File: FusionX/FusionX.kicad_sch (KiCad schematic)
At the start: 1 part, among them U1 SC600YNAPA-E53-UGADA

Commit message: Updated sheet
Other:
- company: (none) -> NoahGWood
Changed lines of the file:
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@@
     (date "2023-08-15")
     (rev "1")
+    (company "NoahGWood")
     (comment 1 "License: The Unlicense")
-    (comment 3 "Twitch.tv")
+    (comment 2 "twitch.tv/u/noahgwood")
+    (comment 3 "Developed Live On:")
     (comment 4 "SC600Y Based Smartphone")
   )

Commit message: Finished RaspiLCD Added Antennas Started secondary LCD
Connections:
- net ANT_WIFI: now reaches U1.129 (ANT_WIFI/BT)
- net ANT_GNSS: now reaches U1.134 (ANT_GNSS)
- net ANT_DRX: now reaches U1.149 (ANT_DRX)
- net LDO6_1P8: now reaches U1.10 (LDO6_1P8)
- net LDO10_2P8: now reaches U1.11 (LDO10_2P8)
- net LDO17_2P85: now reaches U1.12 (LDO17_2P85)
- net LDO2_1P1: now reaches U1.13 (LDO2_1P1)
- net LDO22_2P8: now reaches U1.14 (LDO22_2P8)
- net LDO23_1P2: now reaches U1.15 (LDO23_1P2)
- net VRTC: now reaches U1.16 (VRTC)
- net ANT_MAIN: now reaches U1.19 (ANT_MAIN)
- net +BATT: now reaches U1.27 (BAT_PLUS)
- net -BATT: now reaches U1.28 (BAT_MINUS)
- net BAT_THERM: now reaches U1.29 (BAT_THERM)
- net VBAT: now reaches U1.36 (VBAT)
- net VBAT: now also U1.37 (VBAT), U1.38 (VBAT)
- net LDO5_1P8: now reaches U1.9 (LDO5_1P8)
- net ANT_FM: now reaches U1.244 (ANT_FM)
- no-connect marks 2 -> 4
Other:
- sheet LCD renamed RaspiLCD
- added sheet OtherLCD (OtherLCD.kicad_sch)
- added sheet RF (RF.kicad_sch)
- sheet RaspiLCD: file LCD.kicad_sch -> RaspiLCD.kicad_sch
- moved on the sheet: U1A, U1B, U1C

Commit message: Implemented: 	USB-C Super Speed 	Capacitve Touch Screen 	Secondary LCD
Started On:
	PCB Layout
	Case Design
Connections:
- net USB_SS_RX_P: now reaches U1.171 (USB_SS_RX_P)
- net USB_SS_RX_M: now reaches U1.172 (USB_SS_RX_M)
- net USB_SS_TX_P: now reaches U1.174 (USB_SS_TX__P)
- net USB_SS_TX_M: now reaches U1.175 (USB_SS_TX__M)
- net USB_OPT: now reaches U1.217 (USB_OPT)
- net USB_CC2: now reaches U1.223 (USBC_CC2)
- net USB_CC1: now reaches U1.224 (USBC_CC1)
- net USB_SS_SEL: now reaches U1.226 (USB_SS_SEL)
- net USB_ID: now reaches U1.30 (USB_ID)
- net USB_DP: now reaches U1.32 (USB_DP)
- net USB_DM: now reaches U1.33 (USB_DM)
- net USB_OTG_ON: now reaches U1.247 (GPIO_1)
- net USB_SS_ON: now reaches U1.248 (GPIO_0)
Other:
- added sheet USB (USB.kicad_sch)
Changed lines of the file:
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@@
   (title_block
     (title "FusionX")
-    (date "2023-08-15")
+    (date "2023-08-17")
     (rev "1")
     (company "NoahGWood")
@@
     (stroke (width 0) (type default))
   )
+  (wire (pts (xy 71.755 158.115) (xy 78.105 158.115))
+    (stroke (width 0) (type default))
+  )
   (wire (pts (xy 480.695 204.47) (xy 480.695 207.01))
     (stroke (width 0) (type default))
@@
     (stroke (width 0) (type default))
   )
+  (wire (pts (xy 365.125 156.845) (xy 358.775 156.845))
+    (stroke (width 0) (type default))
+  )
   (wire (pts (xy 531.495 209.55) (xy 531.495 212.09))
     (stroke (width 0) (type default))
@@
     (stroke (width 0) (type default))
   )
+  (wire (pts (xy 365.125 133.985) (xy 358.775 133.985))
+    (stroke (width 0) (type default))
+  )
   (wire (pts (xy 531.495 204.47) (xy 531.495 207.01))
     (stroke (width 0) (type default))
@@
     (stroke (width 0) (type default))
   )
+  (wire (pts (xy 71.755 160.655) (xy 78.105 160.655))
+    (stroke (width 0) (type default))
+  )
   (wire (pts (xy 285.115 303.53) (xy 278.765 303.53))
     (stroke (width 0) (type default))
@@
     (stroke (width 0) (type default))
   )
+  (wire (pts (xy 365.125 141.605) (xy 358.775 141.605))
+    (stroke (width 0) (type default))
+  )
   (wire (pts (xy 480.695 194.31) (xy 480.695 196.85))
     (stroke (width 0) (type default))
@@
     (stroke (width 0) (type default))
   )
+  (wire (pts (xy 71.755 153.035) (xy 78.105 153.035))
+    (stroke (width 0) (type default))
+  )
+  (wire (pts (xy 281.305 118.745) (xy 287.655 118.745))
+    (stroke (width 0) (type default))
+  )
+  (wire (pts (xy 365.125 139.065) (xy 358.775 139.065))
+    (stroke (width 0) (type default))
+  )
   (wire (pts (xy 480.695 232.41) (xy 480.695 234.95))
     (stroke (width 0) (type default))
@@
     (stroke (width 0) (type default))
   )
+  (wire (pts (xy 281.305 113.665) (xy 287.655 113.665))
+    (stroke (width 0) (type default))
+  )
   (wire (pts (xy 196.215 331.47) (xy 202.565 331.47))
     (stroke (width 0) (type default))
@@
     (stroke (width 0) (type default))
   )
+  (wire (pts (xy 281.305 111.125) (xy 287.655 111.125))
+    (stroke (width 0) (type default))
+  )
   (wire (pts (xy 531.495 171.45) (xy 531.495 173.99))
     (stroke (width 0) (type default))
   )
+  (wire (pts (xy 281.305 121.285) (xy 287.655 121.285))
+    (stroke (width 0) (type default))
+  )
   (wire (pts (xy 531.495 224.79) (xy 531.495 227.33))
     (stroke (width 0) (type default))
@@
     (stroke (width 0) (type default))
   )
-  (text_box "TODO:\n	[ ] Microphone\n	[ ] Speaker(s)\n	[ ] Headphone Jack\n	[ ] Antennas\n	[ ] USB-C 3.0\n	[ ] uSIM\n	[ ] SD Card\n	[X] Main LCD\n	[ ] Front Camera\n	[ ] Rear Camera\n	[ ] *Depth Camera\n	[ ] *Secondary Screen\n	[ ] Capacitive Touch\n	[ ] Ambient Light Sensor\n	[ ] Accelerometer\n	[ ] Compass"
+  (text_box "TODO:\n	[ ] Microphone\n	[ ] Speaker(s)\n	[ ] Headphone Jack\n	[X] Antennas\n	[X] USB-C 3.0\n	[ ] uSIM\n	[ ] SD Card\n	[X] Main LCD\n	[ ] Front Camera\n	[ ] Rear Camera\n	[ ] *Depth Camera\n	[ ] *Secondary Screen\n	[X] Capacitive Touch\n	[ ] Ambient Light Sensor\n	[ ] Accelerometer\n	[ ] Compass"
     (at 167.64 47.625 0) (size 66.675 72.39)
     (stroke (width 0) (type default))
     (fill (type none))
     (effects (font (size 2.5 2.5)) (justify left top))
+  )
+  (global_label "USB_SS_TX_M" (shape input) (at 281.305 121.285 180) (fields_autoplaced)
+    (effects (font (size 1.27 1.27)) (justify right))
+    (property "Intersheetrefs" "${INTERSHEET_REFS}" (at 265.5595 121.285 0)
+      (effects (font (size 1.27 1.27)) (justify right) hide)
+    )
+  )
+  (global_label "USB_SS_RX_P" (shape input) (at 281.305 111.125 180) (fields_autoplaced)
+    (effects (font (size 1.27 1.27)) (justify right))
+    (property "Intersheetrefs" "${INTERSHEET_REFS}" (at 265.4385 111.125 0)
+      (effects (font (size 1.27 1.27)) (justify right) hide)
+    )
   )
   (global_label "ANT_GNSS" (shape input) (at 285.115 318.77 0) (fields_autoplaced)
@@
     )
   )
+  (global_label "USB_SS_TX_P" (shape input) (at 281.305 118.745 180) (fields_autoplaced)
+    (effects (font (size 1.27 1.27)) (justify right))
+    (property "Intersheetrefs" "${INTERSHEET_REFS}" (at 265.7409 118.745 0)
+      (effects (font (size 1.27 1.27)) (justify right) hide)
+    )
+  )
   (global_label "VRTC" (shape input) (at 78.105 117.475 180) (fields_autoplaced)
     (effects (font (size 1.27 1.27)) (justify right))
@@
     )
   )
+  (global_label "USB_SS_ON" (shape input) (at 480.695 146.05 180) (fields_autoplaced)
+    (effects (font (size 1.27 1.27)) (justify right))
+    (property "Intersheetrefs" "${INTERSHEET_REFS}" (at 466.8846 146.05 0)
+      (effects (font (size 1.27 1.27)) (justify right) hide)
+    )
+  )
   (global_label "DSI0_LN3_N" (shape output) (at 285.115 344.17 0) (fields_autoplaced)
     (effects (font (size 1.27 1.27)) (justify left))
@@
     )
   )
+  (global_label "USB_SS_RX_M" (shape input) (at 281.305 113.665 180) (fields_autoplaced)
+    (effects (font (size 1.27 1.27)) (justify right))
+    (property "Intersheetrefs" "${INTERSHEET_REFS}" (at 265.2571 113.665 0)
+      (effects (font (size 1.27 1.27)) (justify right) hide)
+    )
+  )
   (global_label "ANT_DRX" (shape input) (at 285.242 280.67 0) (fields_autoplaced)
     (effects (font (size 1.27 1.27)) (justify left))
@@
     )
   )
+  (global_label "USB_SS_SEL" (shape input) (at 365.125 133.985 0) (fields_autoplaced)
+    (effects (font (size 1.27 1.27)) (justify left))
+    (property "Intersheetrefs" "${INTERSHEET_REFS}" (at 379.661 133.985 0)
+      (effects (font (size 1.27 1.27)) (justify left) hide)
+    )
+  )
+  (global_label "USB_DM" (shape input) (at 71.755 160.655 180) (fields_autoplaced)
+    (effects (font (size 1.27 1.27)) (justify right))
+    (property "Intersheetrefs" "${INTERSHEET_REFS}" (at 61.2708 160.655 0)
+      (effects (font (size 1.27 1.27)) (justify right) hide)
+    )
+  )
   (global_label "ANT_MAIN" (shape input) (at 71.755 125.095 180) (fields_autoplaced)
     (effects (font (size 1.27 1.27)) (justify right))
@@
     )
   )
+  (global_label "USB_OTG_ON" (shape input) (at 480.695 143.51 180) (fields_autoplaced)
+    (effects (font (size 1.27 1.27)) (justify right))
+    (property "Intersheetrefs" "${INTERSHEET_REFS}" (at 465.7355 143.51 0)
+      (effects (font (size 1.27 1.27)) (justify right) hide)
+    )
+  )
   (global_label "DSI0_LN1_P" (shape output) (at 196.215 341.63 180) (fields_autoplaced)
     (effects (font (size 1.27 1.27)) (justify right))
@@
     )
   )
+  (global_label "USB_ID" (shape input) (at 71.755 153.035 180) (fields_autoplaced)
+    (effects (font (size 1.27 1.27)) (justify right))
+    (property "Intersheetrefs" "${INTERSHEET_REFS}" (at 62.1174 153.035 0)
+      (effects (font (size 1.27 1.27)) (justify right) hide)
+    )
+  )
   (global_label "LDO2_1P1" (shape passive) (at 78.105 109.855 180) (fields_autoplaced)
     (effects (font (size 1.27 1.27)) (justify right))
@@
     )
   )
+  (global_label "USB_CC2" (shape input) (at 365.125 141.605 0) (fields_autoplaced)
+    (effects (font (size 1.27 1.27)) (justify left))
+    (property "Intersheetrefs" "${INTERSHEET_REFS}" (at 376.6373 141.605 0)
+      (effects (font (size 1.27 1.27)) (justify left) hide)
+    )
+  )
+  (global_label "USB_DP" (shape input) (at 71.755 158.115 180) (fields_autoplaced)
+    (effects (font (size 1.27 1.27)) (justify right))
+    (property "Intersheetrefs" "${INTERSHEET_REFS}" (at 61.4522 158.115 0)
+      (effects (font (size 1.27 1.27)) (justify right) hide)
+    )
+  )
+  (global_label "USB_CC1" (shape input) (at 365.125 139.065 0) (fields_autoplaced)
+    (effects (font (size 1.27 1.27)) (justify left))
+    (property "Intersheetrefs" "${INTERSHEET_REFS}" (at 376.6373 139.065 0)
+      (effects (font (size 1.27 1.27)) (justify left) hide)
+    )
+  )
   (global_label "LDO6_1P8" (shape passive) (at 78.105 102.235 180) (fields_autoplaced)
     (effects (font (size 1.27 1.27)) (justify right))
     (property "Intersheetrefs" "${INTERSHEET_REFS}" (at 66.7364 102.235 0)
       (effects (font (size 1.27 1.27)) (justify right) hide)
+    )
+  )
+  (global_label "USB_OPT" (shape input) (at 365.125 156.845 0) (fields_autoplaced)
+    (effects (font (size 1.27 1.27)) (justify left))
+    (property "Intersheetrefs" "${INTERSHEET_REFS}" (at 376.4559 156.845 0)
+      (effects (font (size 1.27 1.27)) (justify left) hide)
     )
   )
@@
     )
   )
-  (sheet (at 499.11 26.67) (size 43.18 36.83) (fields_autoplaced)
+  (sheet (at 481.5332 30.3784) (size 43.18 36.83) (fields_autoplaced)
     (stroke (width 0.1524) (type solid))
     (fill (color 0 0 0 0.0000))
-    (property "Sheetname" "Power" (at 499.11 25.9584 0)
+    (property "Sheetname" "Power" (at 481.5332 29.6668 0)
       (effects (font (size 1.27 1.27)) (justify left bottom))
     )
-    (property "Sheetfile" "power.kicad_sch" (at 499.11 64.0846 0)
+    (property "Sheetfile" "power.kicad_sch" (at 481.5332 67.793 0)
       (effects (font (size 1.27 1.27)) (justify left top))
     )
@@
       )
     )
+  )
+  (sheet (at 546.7096 54.2036) (size 15.7988 21.7424) (fields_autoplaced)
+    (stroke (width 0.1524) (type solid))
+    (fill (color 0 0 0 0.0000))
+    (property "Sheetname" "USB" (at 546.7096 53.492 0)
+      (effects (font (size 1.27 1.27)) (justify left bottom))
+    )
+    (property "Sheetfile" "USB.kicad_sch" (at 546.7096 76.5306 0)
+      (effects (font (size 1.27 1.27)) (justify left top))
+    )
+    (instances
+      (project "FusionX"
+        (path "/91d1c248-6dd5-47d7-a0ee-1ed6541bbbfb" (page "6"))
+      )
+    )

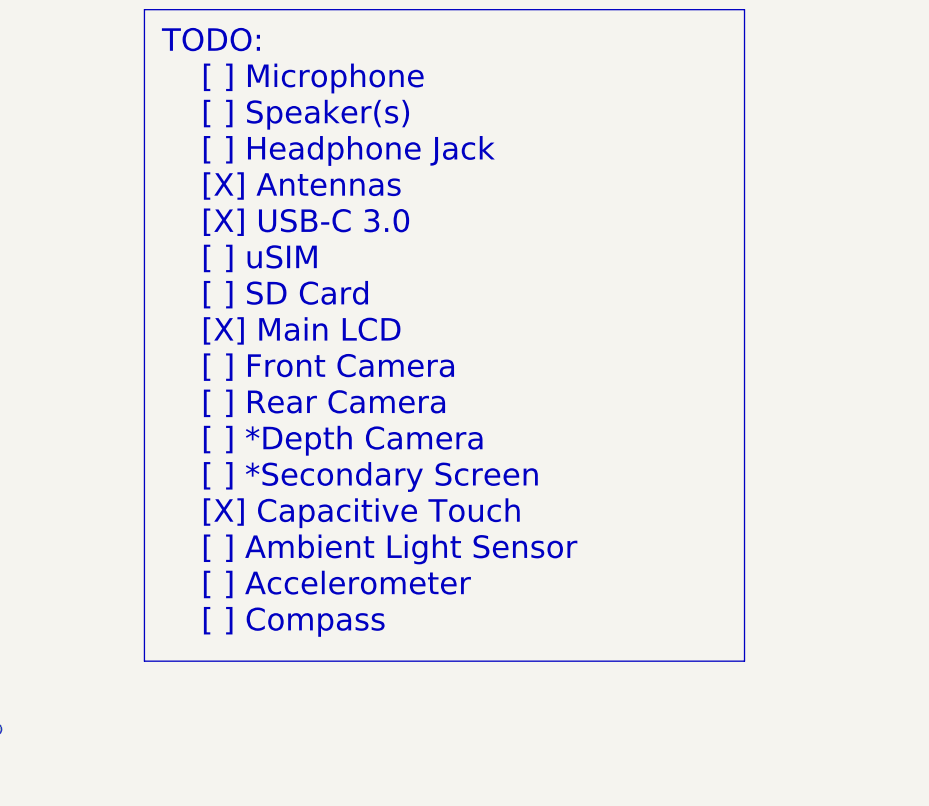
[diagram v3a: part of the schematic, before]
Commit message: Removed unneeded files
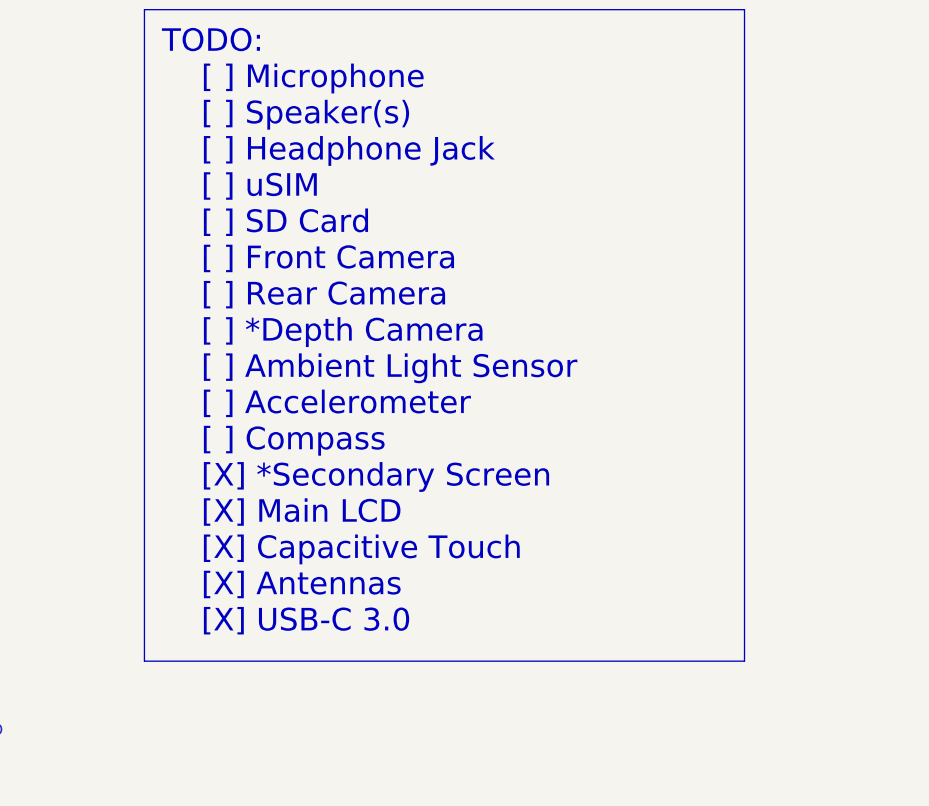
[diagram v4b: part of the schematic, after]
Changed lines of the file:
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@@
     (stroke (width 0) (type default))
   )
-  (text_box "TODO:\n	[ ] Microphone\n	[ ] Speaker(s)\n	[ ] Headphone Jack\n	[X] Antennas\n	[X] USB-C 3.0\n	[ ] uSIM\n	[ ] SD Card\n	[X] Main LCD\n	[ ] Front Camera\n	[ ] Rear Camera\n	[ ] *Depth Camera\n	[ ] *Secondary Screen\n	[X] Capacitive Touch\n	[ ] Ambient Light Sensor\n	[ ] Accelerometer\n	[ ] Compass"
+  (text_box "TODO:\n	[ ] Microphone\n	[ ] Speaker(s)\n	[ ] Headphone Jack\n	[ ] uSIM\n	[ ] SD Card\n	[ ] Front Camera\n	[ ] Rear Camera\n	[ ] *Depth Camera\n	[ ] Ambient Light Sensor\n	[ ] Accelerometer\n	[ ] Compass\n	[X] *Secondary Screen\n	[X] Main LCD\n	[X] Capacitive Touch\n	[X] Antennas\n	[X] USB-C 3.0\n"
     (at 167.64 47.625 0) (size 66.675 72.39)
     (stroke (width 0) (type default))
